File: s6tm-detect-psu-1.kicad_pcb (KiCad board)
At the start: 4 copper layers, 115 parts, among them J1 Conn_01x02, J2 Conn_01x02, J3 USB_C_Receptacle_USB2.0_14P, J4 Conn_01x04, J5 Conn_01x04, J6 Conn_01x04_Pin, J7 TC2030, SW1 SW_Push, SW2 SW_Push, U1 TPS259470x, U2 TPS259470x, U3 TPS259470x, U4 TPS62933, U5 TPS259470x, U6 SN65HVD230, U7 HT753-1, U8 STM32F103C8Tx, Y1 8M

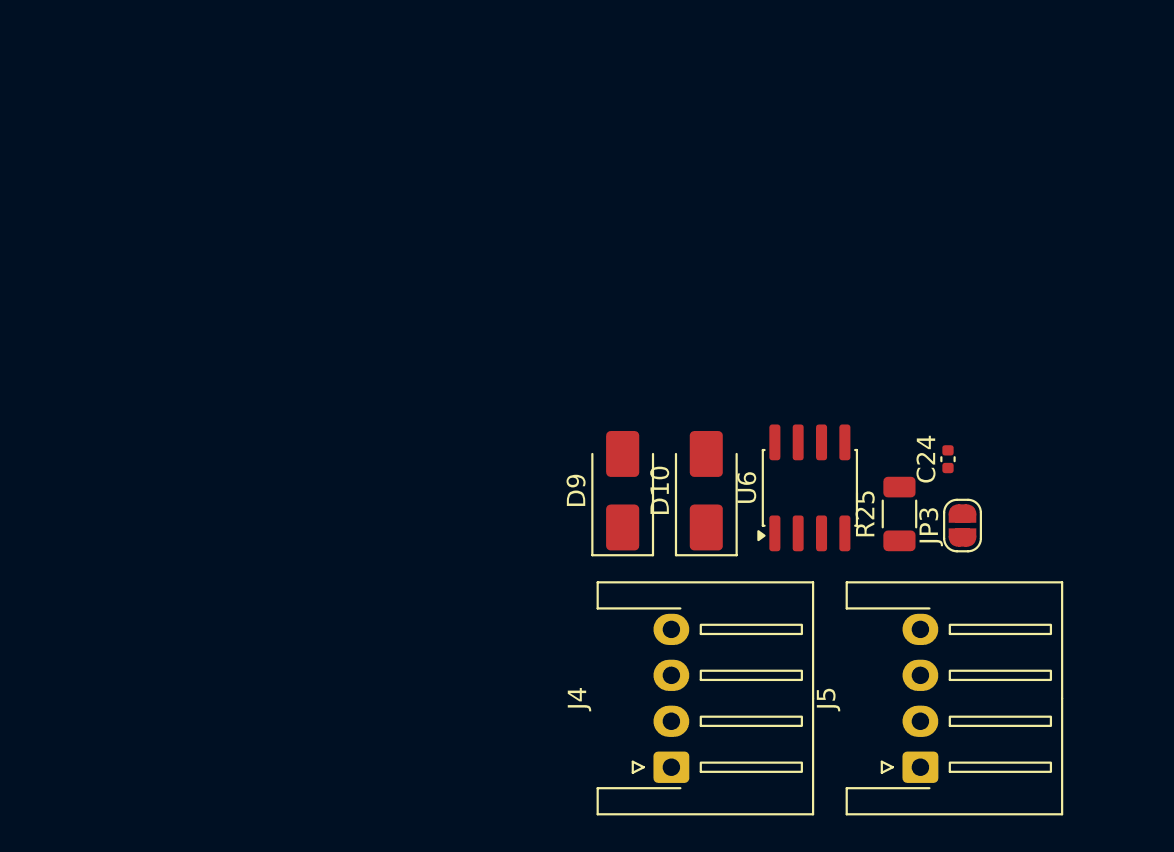
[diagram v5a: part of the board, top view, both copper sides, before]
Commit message: pcb: add can layout
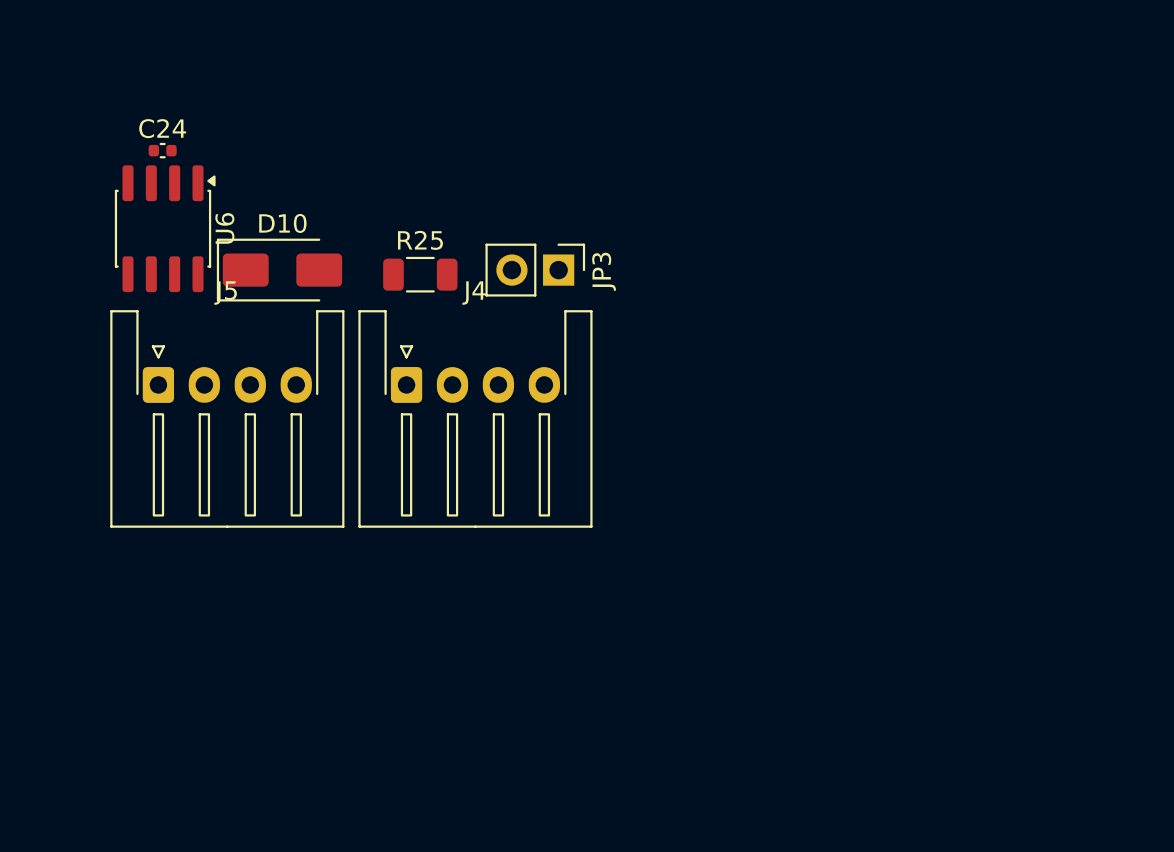
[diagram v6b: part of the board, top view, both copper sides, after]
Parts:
- removed D9: SMBJ6.0CA, Diode_SMD:D_SMA
- JP3: footprint Jumper:SolderJumper-2_P1.3mm_Open_RoundedPad1.0x1.5mm -> Connector_PinHeader_2.54mm:PinHeader_1x02_P2.54mm_Vertical
- moved J5 46.4 mm to (211.5, 130.0), turned to 0 degrees
- moved C24 45.9 mm to (211.7, 117.2), turned to 0 degrees
- moved U6 37.9 mm to (211.8, 121.5), turned to -90 degrees
- moved R25 29.1 mm to (225.8, 124.0), turned to 0 degrees
- moved JP3 26.0 mm to (233.3, 123.8), turned to -90 degrees
- moved D10 26.0 mm to (218.2, 123.8), turned to 0 degrees
- moved J4 25.3 mm to (225.0, 130.0), turned to 0 degrees

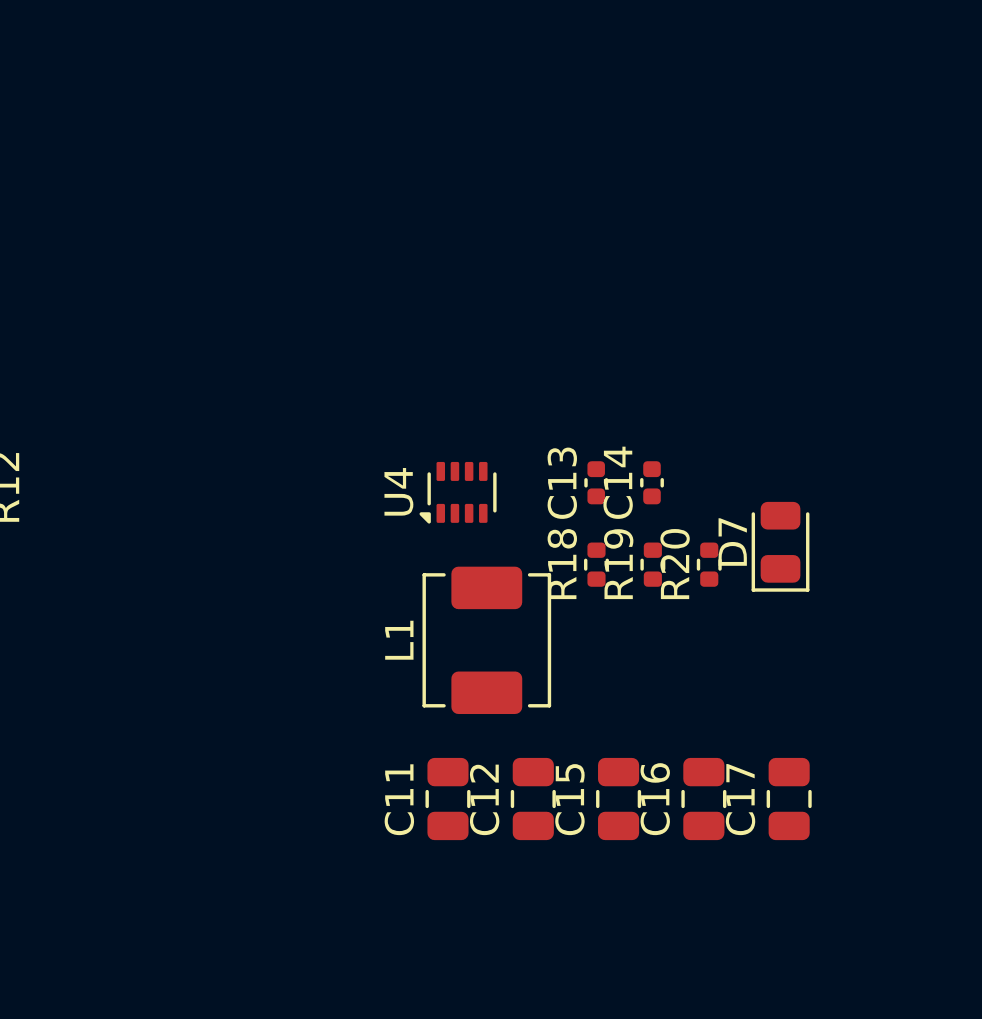
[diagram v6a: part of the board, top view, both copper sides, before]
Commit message: pcb: add smps layout
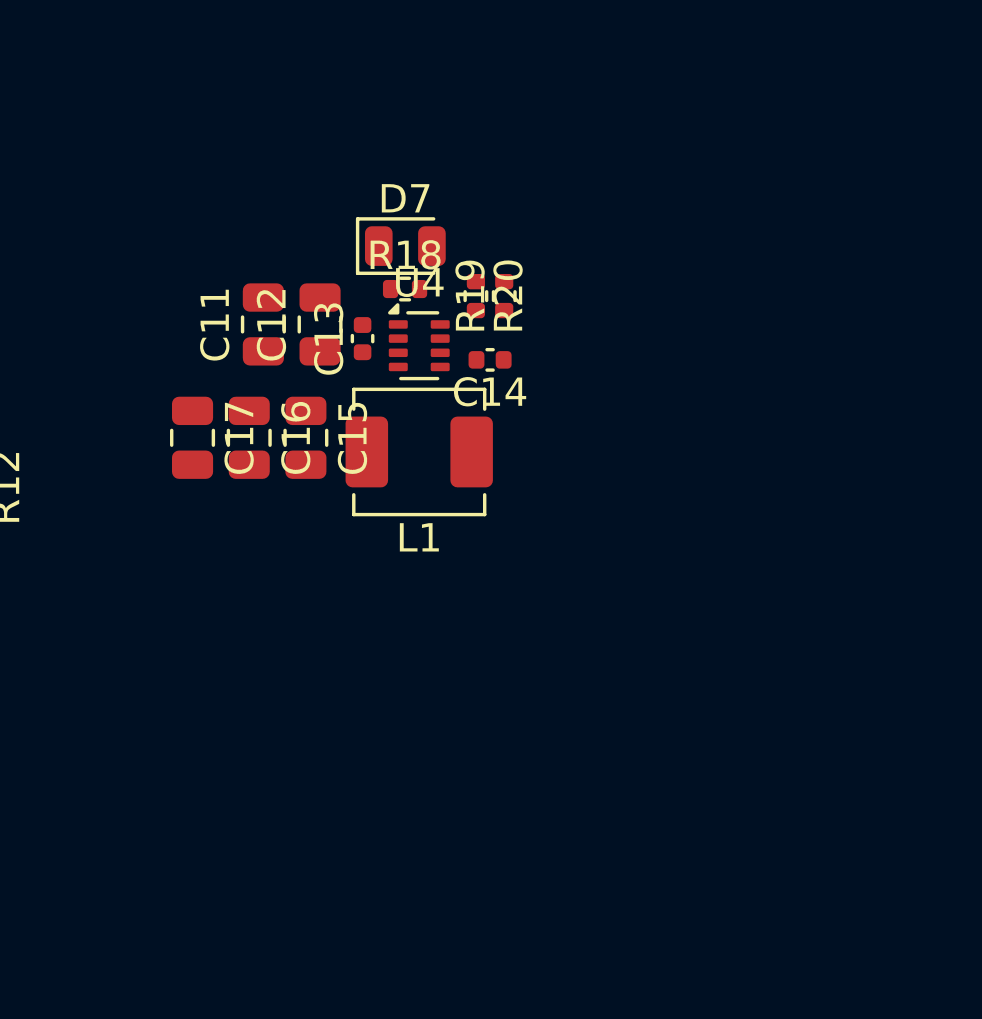
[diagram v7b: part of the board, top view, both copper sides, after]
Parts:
- moved C17 24.6 mm to (122.2, 67.2), turned to -90 degrees
- moved C16 20.5 mm to (124.2, 67.2), turned to -90 degrees
- moved C12 18.4 mm to (126.8, 63.2)
- moved C11 18.0 mm to (124.8, 63.2)
- moved D7 16.9 mm to (129.8, 60.5), turned to 0 degrees
- moved C15 16.9 mm to (126.2, 67.2), turned to -90 degrees
- moved R20 12.6 mm to (132.2, 62.2), turned to -90 degrees
- moved R18 11.8 mm to (129.8, 62.0), turned to 0 degrees
- moved R19 10.8 mm to (133.2, 62.2)
- moved C13 9.69 mm to (128.2, 63.8)
- moved C14 7.17 mm to (132.8, 64.5), turned to 180 degrees
- moved L1 7.06 mm to (130.2, 67.8), turned to 180 degrees
- moved U4 5.39 mm to (130.2, 64.0), turned to 0 degrees

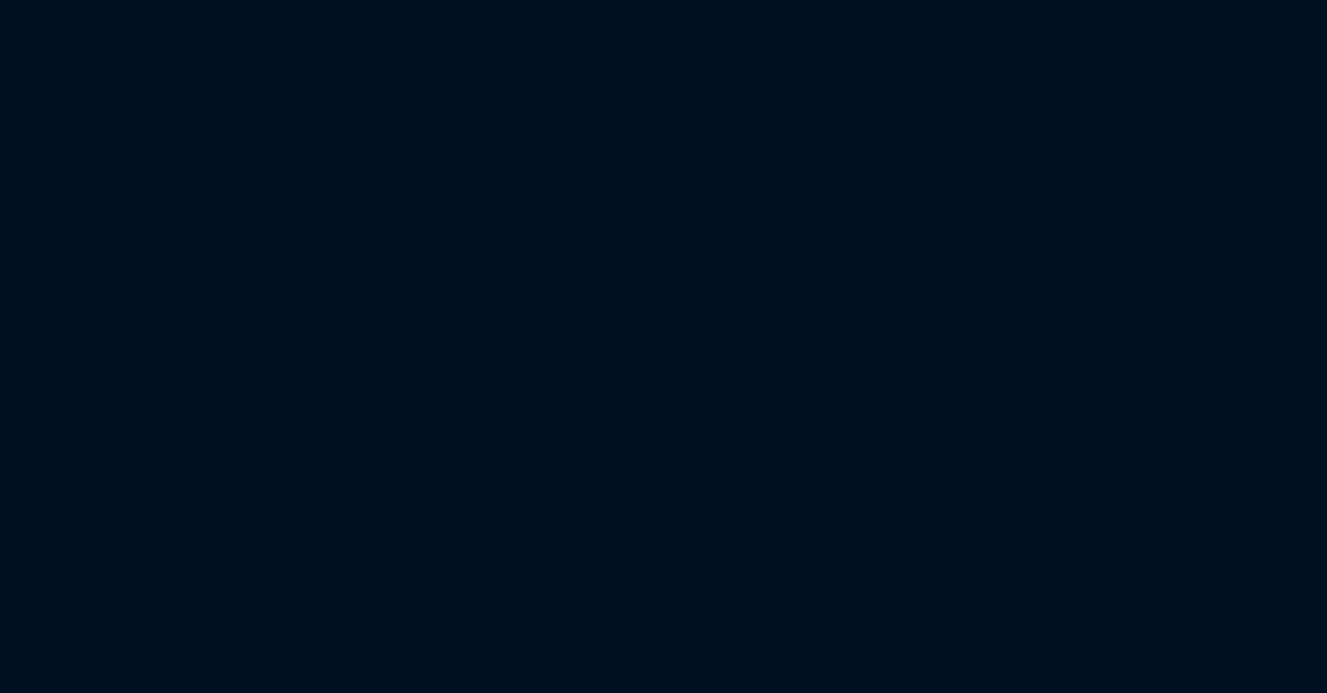
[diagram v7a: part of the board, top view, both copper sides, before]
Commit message: schem/pcb: add mouting and tooling holes
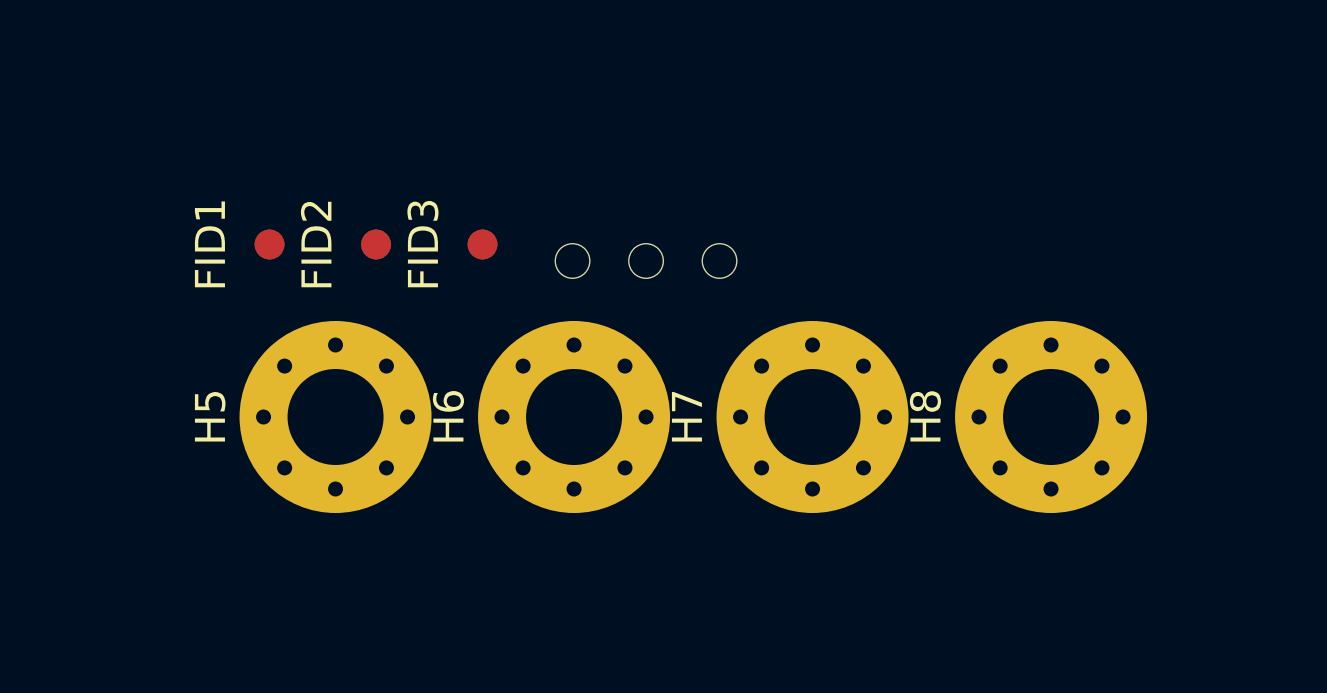
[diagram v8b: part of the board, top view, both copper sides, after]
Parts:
- added FID1: Fiducial, Fiducial:Fiducial_1mm_Mask2mm, F.Cu at (135.0, 88.8)
- added FID2: Fiducial, Fiducial:Fiducial_1mm_Mask2mm, F.Cu at (138.6, 88.8)
- added FID3: Fiducial, Fiducial:Fiducial_1mm_Mask2mm, F.Cu at (142.1, 88.8)
- added H1: MountingHole, MountingHole:ToolingHole_1.152mm, F.Cu at (145.1, 89.3)
- added H2: MountingHole, MountingHole:ToolingHole_1.152mm, F.Cu at (147.6, 89.3)
- added H3: MountingHole, MountingHole:ToolingHole_1.152mm, F.Cu at (150.0, 89.3)
- added H5: MountingHole_Pad, MountingHole:MountingHole_3.2mm_M3_Pad_Via, F.Cu at (137.2, 94.5)
- added H6: MountingHole_Pad, MountingHole:MountingHole_3.2mm_M3_Pad_Via, F.Cu at (145.2, 94.5)
- added H7: MountingHole_Pad, MountingHole:MountingHole_3.2mm_M3_Pad_Via, F.Cu at (153.1, 94.5)
- added H8: MountingHole_Pad, MountingHole:MountingHole_3.2mm_M3_Pad_Via, F.Cu at (161.1, 94.5)
